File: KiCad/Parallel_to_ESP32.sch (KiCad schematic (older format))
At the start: 9 parts, among them J1 DB25_Male, J3 Micro_SD_Card_Socket, U1 ESP32-DEVKIT-V1

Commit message: placing of components and some routing done
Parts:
- added U?: SN74CB3T16210, Package_SO:TSSOP-48_6.1x12.5mm_P0.5mm, symbol Parallel_to_ESP32:SN74CB3T16210
- renumbered C4 to C1
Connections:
- net labels added: +3V3, CD
- net labels removed: +5V, CP, SS
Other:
- moved on the sheet: J1, U1

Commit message: more routing done
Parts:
- gave numbers to parts that had none: 1
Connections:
- net labels added: ACK_3V3, Amiga_5V, BUSY_3V3, D0_3V3, D1_3V3, D2_3V3, D3_3V3, D4_3V3, D5_3V3, D6_3V3, D7_3V3, POUT_3V3, RESET_3V3, SELECT_3V3, STROBE, STROBE_3V3
- net labels removed: VCC
- wire segments 22 -> 26
- no-connect marks 8 -> 13
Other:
- moved on the sheet: JP1, U1
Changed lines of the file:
@@
 Text GLabel 1550 4900 0    50   Output ~ 0
 RESET
-Text GLabel 5650 5200 2    50   Input ~ 0
-GND
-Text GLabel 4900 2250 0    50   BiDi ~ 0
+Text GLabel 5900 5200 2    50   Input ~ 0
+GND
+Text GLabel 2750 5150 0    50   BiDi ~ 0
 BUSY
-Text GLabel 4900 2350 0    50   BiDi ~ 0
+Text GLabel 2750 5250 0    50   BiDi ~ 0
 POUT
-Text GLabel 5450 1950 2    50   BiDi ~ 0
+Text GLabel 2750 4050 0    50   BiDi ~ 0
 D6
-Text GLabel 5450 1850 2    50   BiDi ~ 0
+Text GLabel 2750 4150 0    50   BiDi ~ 0
 D7
-Text GLabel 5450 2550 2    50   BiDi ~ 0
+Text GLabel 2750 3350 0    50   BiDi ~ 0
 D0
-Text GLabel 5450 2450 2    50   BiDi ~ 0
+Text GLabel 2750 3450 0    50   BiDi ~ 0
 D1
-Text GLabel 5450 2350 2    50   BiDi ~ 0
+Text GLabel 2750 3550 0    50   BiDi ~ 0
 D2
-Text GLabel 5450 2250 2    50   BiDi ~ 0
+Text GLabel 2750 3650 0    50   BiDi ~ 0
 D3
-Text GLabel 5450 2150 2    50   BiDi ~ 0
+Text GLabel 2750 3850 0    50   BiDi ~ 0
 D4
-Text GLabel 5450 2050 2    50   BiDi ~ 0
+Text GLabel 2750 3950 0    50   BiDi ~ 0
 D5
-Text GLabel 6700 1550 2    50   Input ~ 0
-RESET
 $Comp
 L power:PWR_FLAG #FLG0101
@@
 Text GLabel 7850 4400 1    50   Input ~ 0
 MOSI
-Text GLabel 4900 2150 0    50   BiDi ~ 0
+Text GLabel 2750 5350 0    50   BiDi ~ 0
 SELECT
 Text GLabel 7650 4400 1    50   Input ~ 0
@@
 NoConn ~ 1550 3500
 NoConn ~ 1550 5100
-Text GLabel 4450 4600 0    50   Output ~ 0
+Text GLabel 4700 4600 0    50   Output ~ 0
 SCK
-Text GLabel 4450 4400 0    50   Input ~ 0
+Text GLabel 4700 4400 0    50   Input ~ 0
 MISO
-Text GLabel 4450 4500 0    50   Output ~ 0
+Text GLabel 4700 4500 0    50   Output ~ 0
 MOSI
 Text GLabel 1600 2450 0    50   Input ~ 0
@@
 Wire Wire Line
 	1250 4500 1250 4700
-Text GLabel 4900 2550 0    50   Output ~ 0
+Text GLabel 2750 5050 0    50   Output ~ 0
 ACK
-NoConn ~ 1550 5400
 $Comp
 L Connector:DB25_Male J1
@@
 Text GLabel 7750 3900 2    50   Input ~ 0
 3V3
-Text GLabel 5650 3200 2    50   Output ~ 0
+Text GLabel 5900 3200 2    50   Output ~ 0
 3V3
 Text GLabel 7150 6100 3    50   Input ~ 0
@@
 Wire Notes Line
 	10500 5100 9100 5100
-Text GLabel 5650 4900 2    50   Input ~ 0
+Text GLabel 5900 4900 2    50   Input ~ 0
 CD
-Text GLabel 4450 4700 0    50   Output ~ 0
+Text GLabel 4700 4700 0    50   Output ~ 0
 CS
 Text GLabel 9550 5900 3    50   Output ~ 0
@@
 Text GLabel 4900 2450 0    50   Input ~ 0
 ACT_LED
-NoConn ~ 1550 5300
 $Comp
 L Device:C_Small C1
@@
 L Jumper:Jumper_2_Open JP1
 U 1 1 611CD315
-P 6500 1550
-F 0 "JP1" H 6500 1693 50  0000 C CNN
-F 1 "Jumper_2_Open" H 6500 1694 50  0001 C CNN
-F 2 "Resistor_SMD:R_1206_3216Metric_Pad1.42x1.75mm_HandSolder" H 6500 1550 50  0001 C CNN
-F 3 "~" H 6500 1550 50  0001 C CNN
-	1    6500 1550
-	1    0    0    -1
-$EndComp
-Wire Wire Line
-	6000 1550 6300 1550
+P 5750 2200
+F 0 "JP1" H 5750 2343 50  0000 C CNN
+F 1 "Jumper_2_Open" H 5750 2344 50  0001 C CNN
+F 2 "Resistor_SMD:R_1206_3216Metric_Pad1.42x1.75mm_HandSolder" H 5750 2200 50  0001 C CNN
+F 3 "~" H 5750 2200 50  0001 C CNN
+	1    5750 2200
+	1    0    0    -1
+$EndComp
 NoConn ~ 8050 4400
 NoConn ~ 7350 4400
@@
 L Parallel_to_ESP32:ESP32-DEVKIT-V1 U1
 U 1 1 643ACCD9
-P 5050 4200
-F 0 "U1" H 5050 5467 50  0000 C CNN
-F 1 "ESP32-DEVKIT-V1" H 5050 5376 50  0000 C CNN
-F 2 "Parallel_to_ESP32:MODULE_ESP32_DEVKIT_V1" H 5050 4200 50  0001 L BNN
-F 3 "" H 5050 4200 50  0001 L BNN
-F 4 "N/A" H 5050 4200 50  0001 L BNN "PARTREV"
-F 5 "6.8 mm" H 5050 4200 50  0001 L BNN "MAXIMUM_PACKAGE_HEIGHT"
-F 6 "Manufacturer Recommendations" H 5050 4200 50  0001 L BNN "STANDARD"
-F 7 "DOIT" H 5050 4200 50  0001 L BNN "MANUFACTURER"
-	1    5050 4200
+P 5300 4200
+F 0 "U1" H 5300 5467 50  0000 C CNN
+F 1 "ESP32-DEVKIT-V1" H 5300 5376 50  0000 C CNN
+F 2 "Parallel_to_ESP32:MODULE_ESP32_DEVKIT_V1" H 5300 4200 50  0001 L BNN
+F 3 "" H 5300 4200 50  0001 L BNN
+F 4 "N/A" H 5300 4200 50  0001 L BNN "PARTREV"
+F 5 "6.8 mm" H 5300 4200 50  0001 L BNN "MAXIMUM_PACKAGE_HEIGHT"
+F 6 "Manufacturer Recommendations" H 5300 4200 50  0001 L BNN "STANDARD"
+F 7 "DOIT" H 5300 4200 50  0001 L BNN "MANUFACTURER"
+	1    5300 4200
 	1    0    0    -1
 $EndComp
@@
 Text GLabel 3750 3750 2    50   Input ~ 0
 GND
-Text GLabel 4450 3200 0    50   Input ~ 0
-VCC
 Text GLabel 2750 4450 0    50   Input ~ 0
 3V3
 $Comp
-L Parallel_to_ESP32:SN74CB3T16210 U?
+L Parallel_to_ESP32:SN74CB3T16210 U2
 U 1 1 6442C4B2
 P 3250 4150
-F 0 "U?" H 3250 5517 50  0000 C CNN
+F 0 "U2" H 3250 5517 50  0000 C CNN
 F 1 "SN74CB3T16210" H 3250 5426 50  0000 C CNN
 F 2 "Package_SO:TSSOP-48_6.1x12.5mm_P0.5mm" H 4900 4600 50  0001 C CNN
@@
 $EndComp
 $Comp
-L power:+3V3 #PWR?
+L power:+3V3 #PWR0101
 U 1 1 644304C8
 P 1600 2400
-F 0 "#PWR?" H 1600 2250 50  0001 C CNN
+F 0 "#PWR0101" H 1600 2250 50  0001 C CNN
 F 1 "+3V3" H 1615 2573 50  0000 C CNN
 F 2 "" H 1600 2400 50  0001 C CNN
@@
 	1    0    0    -1
 $EndComp
+Text GLabel 3750 5350 2    50   BiDi ~ 0
+SELECT_3V3
+Text GLabel 3750 5150 2    50   BiDi ~ 0
+BUSY_3V3
+Text GLabel 3750 5250 2    50   BiDi ~ 0
+POUT_3V3
+Text GLabel 3750 3450 2    50   BiDi ~ 0
+D0_3V3
+Text GLabel 3750 3550 2    50   BiDi ~ 0
+D1_3V3
+Text GLabel 3750 3650 2    50   BiDi ~ 0
+D2_3V3
+Text GLabel 3750 3850 2    50   BiDi ~ 0
+D3_3V3
+Text GLabel 3750 3950 2    50   BiDi ~ 0
+D4_3V3
+Text GLabel 3750 4050 2    50   BiDi ~ 0
+D5_3V3
+Text GLabel 3750 4150 2    50   BiDi ~ 0
+D6_3V3
+Text GLabel 3750 4250 2    50   BiDi ~ 0
+D7_3V3
+Text GLabel 2750 4250 0    50   Input ~ 0
+GND
+Wire Wire Line
+	2750 4250 2750 4350
+Wire Wire Line
+	2750 4550 2750 4650
+Connection ~ 2750 4650
+Wire Wire Line
+	2750 4650 2750 4750
+Connection ~ 2750 4750
+Wire Wire Line
+	2750 4750 2750 4850
+Connection ~ 2750 4850
+Wire Wire Line
+	2750 4850 2750 4950
+NoConn ~ 3750 4350
+NoConn ~ 3750 4450
+NoConn ~ 3750 4550
+NoConn ~ 3750 4750
+NoConn ~ 3750 4850
+NoConn ~ 3750 4950
+Text GLabel 1550 5400 0    50   Output ~ 0
+STROBE
+Text GLabel 1550 5300 0    50   Output ~ 0
+Amiga_5V
+Text GLabel 2750 3250 0    50   Input ~ 0
+STROBE
+Text GLabel 3750 3350 2    50   Output ~ 0
+STROBE_3V3
+Text GLabel 3750 5050 2    50   Input ~ 0
+ACK_3V3
+NoConn ~ 4700 3200
+Text GLabel 2750 3150 0    50   Input ~ 0
+RESET
+Text GLabel 3750 3250 2    50   Output ~ 0
+RESET_3V3
 $EndSCHEMATC

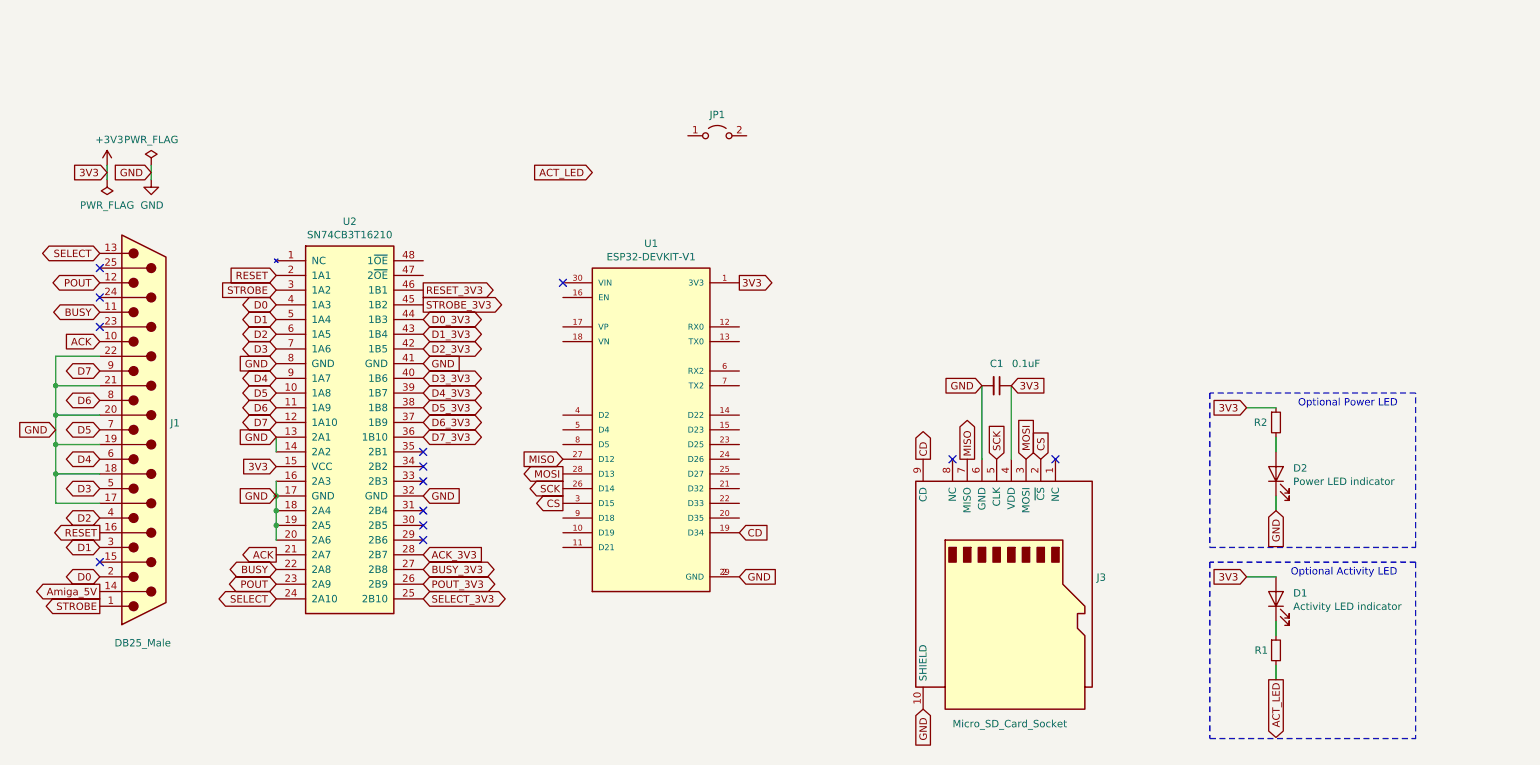
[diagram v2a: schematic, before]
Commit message: more pin assignments and routing
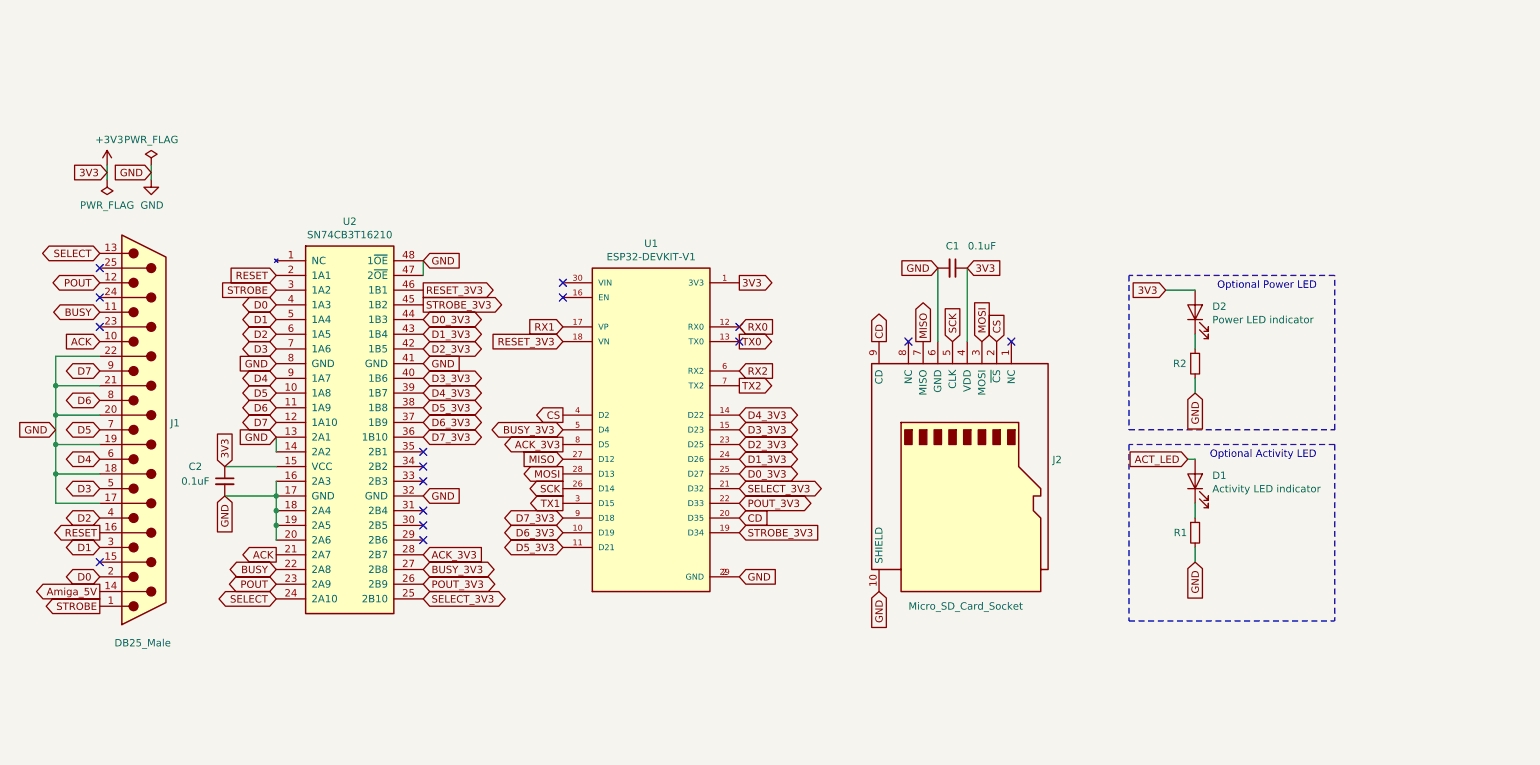
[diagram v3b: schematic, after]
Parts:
- removed JP1: Jumper_2_Open, Resistor_SMD:R_1206_3216Metric_Pad1.42x1.75mm_HandSolder, symbol Jumper:Jumper_2_Open
- added C2: 0.1uF, Capacitor_SMD:C_0805_2012Metric_Pad1.15x1.40mm_HandSolder, symbol Device:C_Small
- renumbered J3 to J2
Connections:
- net +3V3: now also D2.2 (A), C2.1; no longer D1.2 (A), R2.1
- net ACK_3V3: now also U1.8 (D5)
- net ACT_LED: now also D1.2 (A); no longer R1.2
- net BUSY_3V3: now also U1.5 (D4)
- net CD: now also U1.20 (D35); no longer U1.19 (D34)
- net CS: now also U1.4 (D2); no longer U1.3 (D15)
- net D0_3V3: now also U1.25 (D27)
- net D1_3V3: now also U1.24 (D26)
- net D2_3V3: now also U1.23 (D25)
- net D3_3V3: now also U1.15 (D23)
- net D4_3V3: now also U1.14 (D22)
- net D5_3V3: now also U1.11 (D21)
- net D6_3V3: now also U1.10 (D19)
- net D7_3V3: now also U1.9 (D18)
- net GND: now also R1.2, R2.2, U2.47 (2~OE), U2.48 (1~OE), C2.2; no longer D2.1 (K)
- net POUT_3V3: now also U1.22 (D33)
- net RESET_3V3: now also U1.18 (VN)
- net SELECT_3V3: now also U1.21 (D32)
- net STROBE_3V3: now also U1.19 (D34)
- net RX0: now reaches U1.12 (RX0)
- net TX0: now reaches U1.13 (TX0)
- net RX1: now reaches U1.17 (VP)
- net RX2: now reaches U1.6 (RX2)
- net TX2: now reaches U1.7 (TX2)
- new net: D2.1 (K), R2.1
- new net TX1: U1.3 (D15)
- no-connect marks 13 -> 16
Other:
- moved on the sheet: C1, D1, D2, J2, R1, R2
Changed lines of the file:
@@
 Text GLabel 1900 2450 0    50   Input ~ 0
 GND
-Text GLabel 7550 3900 0    50   Input ~ 0
-GND
-Text GLabel 7450 4400 1    50   Output ~ 0
+Text GLabel 7250 3100 0    50   Input ~ 0
+GND
+Text GLabel 7150 3600 1    50   Output ~ 0
 MISO
-Text GLabel 7850 4400 1    50   Input ~ 0
+Text GLabel 7550 3600 1    50   Input ~ 0
 MOSI
 Text GLabel 2750 5350 0    50   BiDi ~ 0
 SELECT
-Text GLabel 7650 4400 1    50   Input ~ 0
+Text GLabel 7350 3600 1    50   Input ~ 0
 SCK
 NoConn ~ 1550 3300
@@
 L Device:LED D2
 U 1 1 5EBAFFCE
-P 9550 4500
-F 0 "D2" V 9589 4383 50  0000 R CNN
-F 1 "Power LED indicator" V 9498 4383 50  0000 R CNN
-F 2 "LED_THT:LED_D3.0mm" H 9550 4500 50  0001 C CNN
-F 3 "~" H 9550 4500 50  0001 C CNN
-	1    9550 4500
+P 9000 3400
+F 0 "D2" V 9039 3283 50  0000 R CNN
+F 1 "Power LED indicator" V 8948 3283 50  0000 R CNN
+F 2 "LED_THT:LED_D3.0mm" H 9000 3400 50  0001 C CNN
+F 3 "~" H 9000 3400 50  0001 C CNN
+	1    9000 3400
 	0    -1   -1   0
 $EndComp
-Text GLabel 9550 4750 3    50   Input ~ 0
-GND
-Wire Wire Line
-	9350 4050 9550 4050
-Wire Wire Line
-	9550 4250 9550 4350
-Wire Wire Line
-	9550 4650 9550 4750
+Text GLabel 9000 3950 3    50   Input ~ 0
+GND
+Wire Wire Line
+	8800 3250 9000 3250
+Wire Wire Line
+	9000 3850 9000 3950
 Text GLabel 1550 3600 0    50   Input ~ 0
 ACK
@@
 L Device:R_Small R2
 U 1 1 5EB9BBF1
-P 9550 4150
-F 0 "R2" H 9400 4150 50  0000 L CNN
-F 1 "150" H 9600 4150 50  0001 L CNN
-F 2 "Resistor_SMD:R_1206_3216Metric_Pad1.42x1.75mm_HandSolder" H 9550 4150 50  0001 C CNN
-F 3 "~" H 9550 4150 50  0001 C CNN
-	1    9550 4150
+P 9000 3750
+F 0 "R2" H 8850 3750 50  0000 L CNN
+F 1 "150" H 9050 3750 50  0001 L CNN
+F 2 "Resistor_SMD:R_1206_3216Metric_Pad1.42x1.75mm_HandSolder" H 9000 3750 50  0001 C CNN
+F 3 "~" H 9000 3750 50  0001 C CNN
+	1    9000 3750
 	1    0    0    -1
 $EndComp
@@
 L Device:R_Small R1
 U 1 1 5EB9CA00
-P 9550 5700
-F 0 "R1" H 9450 5700 50  0000 C CNN
-F 1 "150" H 9700 5700 50  0001 C CNN
-F 2 "Resistor_SMD:R_1206_3216Metric_Pad1.42x1.75mm_HandSolder" H 9550 5700 50  0001 C CNN
-F 3 "~" H 9550 5700 50  0001 C CNN
-	1    9550 5700
+P 9000 4900
+F 0 "R1" H 8900 4900 50  0000 C CNN
+F 1 "150" H 9150 4900 50  0001 C CNN
+F 2 "Resistor_SMD:R_1206_3216Metric_Pad1.42x1.75mm_HandSolder" H 9000 4900 50  0001 C CNN
+F 3 "~" H 9000 4900 50  0001 C CNN
+	1    9000 4900
 	1    0    0    -1
 $EndComp
@@
 L Device:LED D1
 U 1 1 5EBA7223
-P 9550 5350
-F 0 "D1" V 9589 5233 50  0000 R CNN
-F 1 "Activity LED indicator" V 9498 5233 50  0000 R CNN
-F 2 "LED_THT:LED_D3.0mm" H 9550 5350 50  0001 C CNN
-F 3 "~" H 9550 5350 50  0001 C CNN
-	1    9550 5350
+P 9000 4550
+F 0 "D1" V 9039 4433 50  0000 R CNN
+F 1 "Activity LED indicator" V 8948 4433 50  0000 R CNN
+F 2 "LED_THT:LED_D3.0mm" H 9000 4550 50  0001 C CNN
+F 3 "~" H 9000 4550 50  0001 C CNN
+	1    9000 4550
 	0    -1   -1   0
 $EndComp
-Text Notes 9650 5200 0    50   ~ 0
+Text Notes 9100 4400 0    50   ~ 0
 Optional Activity LED
 Wire Notes Line
-	9100 3950 9100 5000
-Wire Notes Line
-	9100 5000 10500 5000
-Wire Notes Line
-	10500 5000 10500 3950
-Wire Notes Line
-	10500 3950 9100 3950
-Text Notes 9700 4050 0    50   ~ 0
+	8550 3150 8550 4200
+Wire Notes Line
+	8550 4200 9950 4200
+Wire Notes Line
+	9950 4200 9950 3150
+Wire Notes Line
+	9950 3150 8550 3150
+Text Notes 9150 3250 0    50   ~ 0
 Optional Power LED
 Wire Wire Line
@@
 $EndComp
 $Comp
-L Parallel_to_ESP32:Micro_SD_Card_Socket J3
+L Parallel_to_ESP32:Micro_SD_Card_Socket J2
 U 1 1 610A01AB
-P 7750 5300
-F 0 "J3" V 7654 5880 50  0000 L CNN
-F 1 "Micro_SD_Card_Socket" V 8650 4900 50  0000 L CNN
-F 2 "Parallel_to_ESP32:GCT-MEM2055-00-190-01-A" H 8900 5600 50  0001 C CNN
-F 3 "" H 7750 5300 50  0001 C CNN
-	1    7750 5300
+P 7450 4500
+F 0 "J2" V 7354 5080 50  0000 L CNN
+F 1 "Micro_SD_Card_Socket" V 8350 4100 50  0000 L CNN
+F 2 "Parallel_to_ESP32:GCT-MEM2055-00-190-01-A" H 8600 4800 50  0001 C CNN
+F 3 "" H 7450 4500 50  0001 C CNN
+	1    7450 4500
 	0    1    1    0
 $EndComp
-Text GLabel 7750 3900 2    50   Input ~ 0
+Text GLabel 7450 3100 2    50   Input ~ 0
 3V3
 Text GLabel 5900 3200 2    50   Output ~ 0
 3V3
-Text GLabel 7150 6100 3    50   Input ~ 0
-GND
-Text GLabel 7950 4400 1    50   Input ~ 0
+Text GLabel 6850 5300 3    50   Input ~ 0
+GND
+Text GLabel 7650 3600 1    50   Input ~ 0
 CS
-Text GLabel 7150 4400 1    50   Output ~ 0
+Text GLabel 6850 3600 1    50   Output ~ 0
 CD
 Wire Wire Line
-	9350 5200 9550 5200
-Wire Wire Line
-	9550 5500 9550 5600
-Wire Wire Line
-	9550 5800 9550 5900
-Wire Notes Line
-	9100 6300 10500 6300
-Wire Notes Line
-	10500 5100 9100 5100
-Text GLabel 5900 4900 2    50   Input ~ 0
+	9000 4700 9000 4800
+Wire Wire Line
+	9000 5000 9000 5100
+Wire Notes Line
+	8550 5500 9950 5500
+Wire Notes Line
+	9950 4300 8550 4300
+Text GLabel 5900 4800 2    50   Input ~ 0
 CD
-Text GLabel 4700 4700 0    50   Output ~ 0
+Text GLabel 4700 4100 0    50   Output ~ 0
 CS
-Text GLabel 9550 5900 3    50   Output ~ 0
+Text GLabel 8950 4400 0    50   Input ~ 0
 ACT_LED
 Wire Notes Line
-	10500 5100 10500 6300
-Wire Notes Line
-	9100 5100 9100 6300
-Text GLabel 4900 2450 0    50   Input ~ 0
-ACT_LED
+	9950 4300 9950 5500
+Wire Notes Line
+	8550 4300 8550 5500
 $Comp
 L Device:C_Small C1
 U 1 1 612089E2
-P 7650 3900
-F 0 "C1" V 7500 3900 50  0000 C CNN
-F 1 "0.1uF" V 7500 4100 50  0000 C CNN
-F 2 "Capacitor_SMD:C_0805_2012Metric_Pad1.15x1.40mm_HandSolder" H 7650 3900 50  0001 C CNN
-F 3 "~" H 7650 3900 50  0001 C CNN
-	1    7650 3900
+P 7350 3100
+F 0 "C1" V 7200 3100 50  0000 C CNN
+F 1 "0.1uF" V 7200 3300 50  0000 C CNN
+F 2 "Capacitor_SMD:C_0805_2012Metric_Pad1.15x1.40mm_HandSolder" H 7350 3100 50  0001 C CNN
+F 3 "~" H 7350 3100 50  0001 C CNN
+	1    7350 3100
 	0    1    1    0
 $EndComp
 Wire Wire Line
-	7550 3900 7550 4400
-Wire Wire Line
-	7750 3900 7750 4400
-$Comp
-L Jumper:Jumper_2_Open JP1
-U 1 1 611CD315
-P 5750 2200
-F 0 "JP1" H 5750 2343 50  0000 C CNN
-F 1 "Jumper_2_Open" H 5750 2344 50  0001 C CNN
-F 2 "Resistor_SMD:R_1206_3216Metric_Pad1.42x1.75mm_HandSolder" H 5750 2200 50  0001 C CNN
-F 3 "~" H 5750 2200 50  0001 C CNN
-	1    5750 2200
-	1    0    0    -1
-$EndComp
-NoConn ~ 8050 4400
-NoConn ~ 7350 4400
+	7250 3100 7250 3600
+Wire Wire Line
+	7450 3100 7450 3600
+NoConn ~ 7750 3600
+NoConn ~ 7050 3600
 $Comp
 L Parallel_to_ESP32:ESP32-DEVKIT-V1 U1
@@
 	1    0    0    -1
 $EndComp
-Text GLabel 9350 4050 0    50   Input ~ 0
-3V3
-Text GLabel 9350 5200 0    50   Input ~ 0
+Text GLabel 8800 3250 0    50   Input ~ 0
 3V3
 Text GLabel 2750 3750 0    50   Input ~ 0
 GND
-Text GLabel 2750 4650 0    50   Input ~ 0
+Text GLabel 2400 4650 3    50   Input ~ 0
 GND
 Text GLabel 3750 4650 2    50   Input ~ 0
@@
 Text GLabel 3750 3750 2    50   Input ~ 0
 GND
-Text GLabel 2750 4450 0    50   Input ~ 0
+Text GLabel 2400 4450 1    50   Input ~ 0
 3V3
 $Comp
@@
 Text GLabel 3750 3250 2    50   Output ~ 0
 RESET_3V3
+$Comp
+L Device:C_Small C2
+U 1 1 6448FFBE
+P 2400 4550
+F 0 "C2" H 2200 4650 50  0000 C CNN
+F 1 "0.1uF" H 2200 4550 50  0000 C CNN
+F 2 "Capacitor_SMD:C_0805_2012Metric_Pad1.15x1.40mm_HandSolder" H 2400 4550 50  0001 C CNN
+F 3 "~" H 2400 4550 50  0001 C CNN
+	1    2400 4550
+	1    0    0    -1
+$EndComp
+Wire Wire Line
+	2400 4450 2750 4450
+Wire Wire Line
+	2400 4650 2750 4650
+Text GLabel 5900 3800 2    50   Input ~ 0
+RX2
+Text GLabel 5900 3900 2    50   Output ~ 0
+TX2
+NoConn ~ 5900 3500
+NoConn ~ 5900 3600
+Wire Wire Line
+	9000 3650 9000 3550
+Wire Wire Line
+	8950 4400 9000 4400
+Text GLabel 9000 5100 3    50   Input ~ 0
+GND
+Text GLabel 4700 3500 0    50   Input ~ 0
+RX1
+Text GLabel 4700 4700 0    50   Output ~ 0
+TX1
+Wire Wire Line
+	3750 3150 3750 3050
+Text GLabel 4700 4300 0    50   Output ~ 0
+ACK_3V3
+Text GLabel 4700 4200 0    50   BiDi ~ 0
+BUSY_3V3
+Text GLabel 5900 4700 2    50   BiDi ~ 0
+POUT_3V3
+Text GLabel 5900 4600 2    50   BiDi ~ 0
+SELECT_3V3
+Text GLabel 5900 4500 2    50   BiDi ~ 0
+D0_3V3
+Text GLabel 5900 4400 2    50   BiDi ~ 0
+D1_3V3
+Text GLabel 5900 4300 2    50   BiDi ~ 0
+D2_3V3
+Text GLabel 5900 4200 2    50   BiDi ~ 0
+D3_3V3
+Text GLabel 5900 4100 2    50   BiDi ~ 0
+D4_3V3
+Text GLabel 4700 5000 0    50   BiDi ~ 0
+D5_3V3
+Text GLabel 4700 4900 0    50   BiDi ~ 0
+D6_3V3
+Text GLabel 4700 4800 0    50   BiDi ~ 0
+D7_3V3
+NoConn ~ 4700 3300
+Text GLabel 5900 3500 2    50   Input ~ 0
+RX0
+Text GLabel 5900 3600 2    50   Output ~ 0
+TX0
+Text GLabel 5900 4900 2    50   Input ~ 0
+STROBE_3V3
+Text GLabel 4700 3600 0    50   Input ~ 0
+RESET_3V3
+Text GLabel 3750 3050 2    50   Input ~ 0
+GND
 $EndSCHEMATC
